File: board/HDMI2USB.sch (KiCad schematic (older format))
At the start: 0 parts

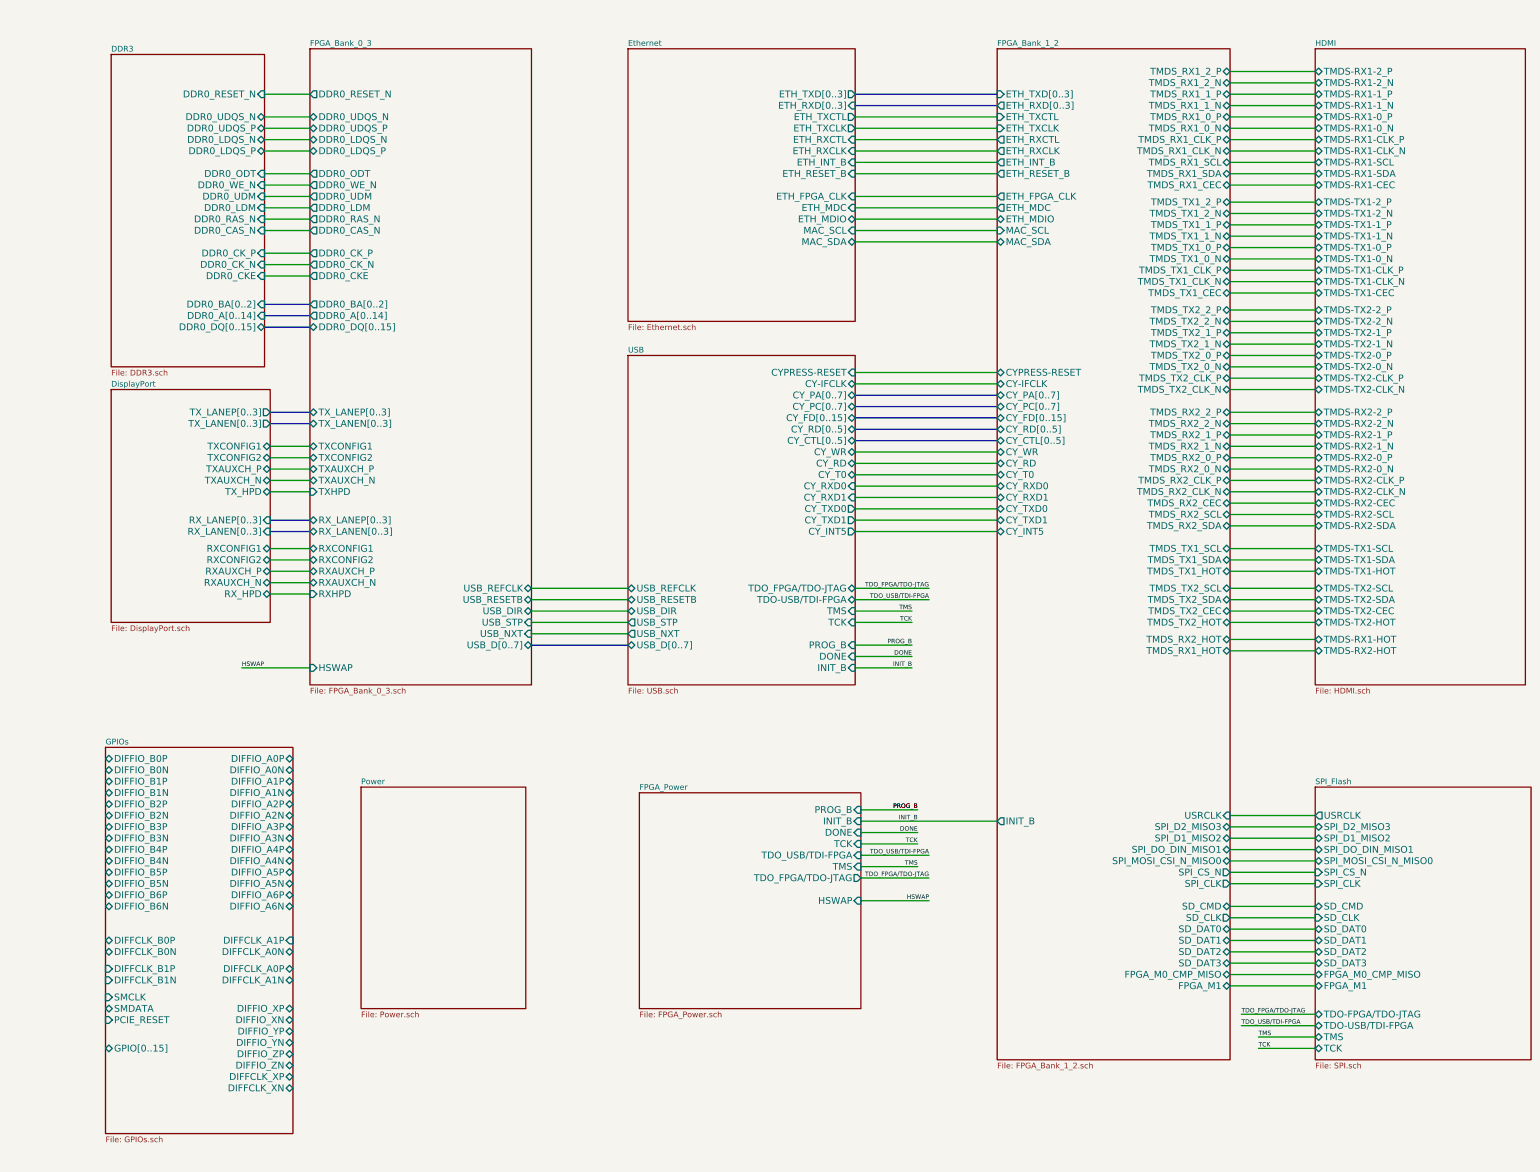
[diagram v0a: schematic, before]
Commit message: Issue #1680 - Bank 0 Ios
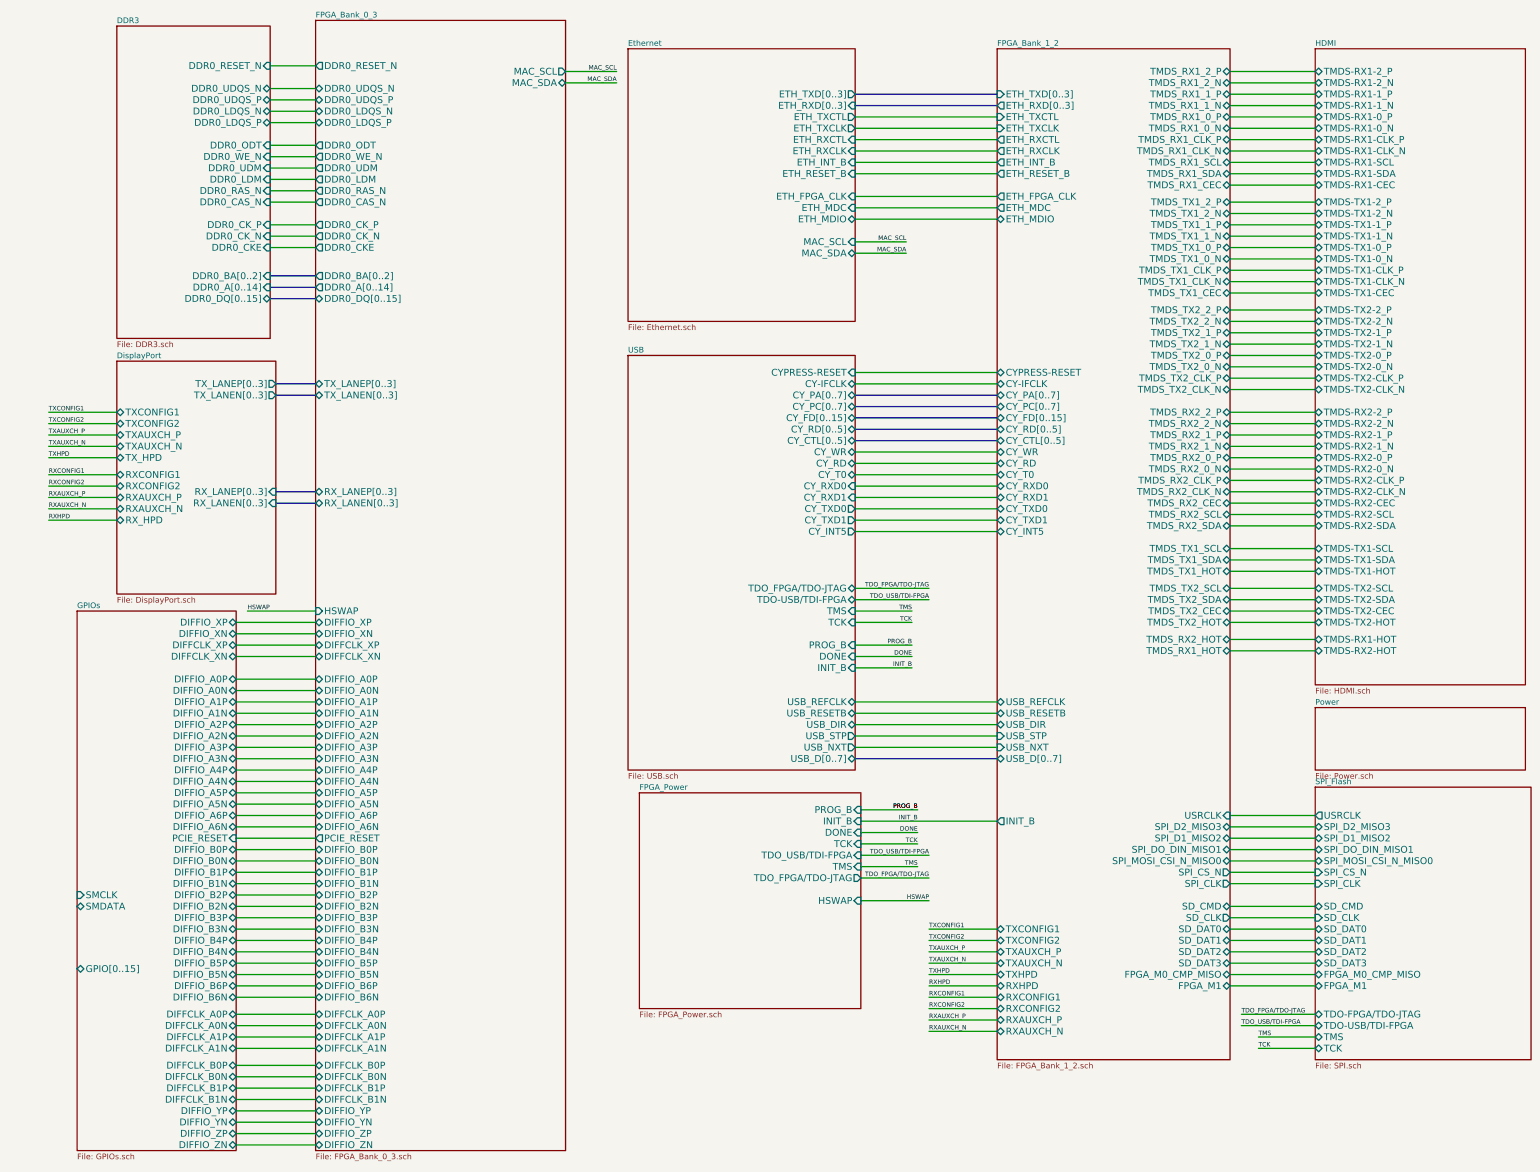
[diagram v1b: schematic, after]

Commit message: Issue #1683
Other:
- note added: "BANK0"
- note added: "BANK1"
- note added: "BANK2"
- note added: "BANK3"
- note added: "CYPRESS/OTG"
- note added: "CYPRESS\nHDMI RX 1\nHDMI RX 2"
- note added: "DDR3"
- note added: "DISPLAY PORT"
- note added: "ETHERNET"
- note added: "FPGA VCC/CONFIG"
- note added: "GTP"
- note added: "HDMI"
- note added: "HDMI TX 1\nHDMI TX 2\nETHERNET\nUTMI\nSPI\nSD\n\n"
- note added: "PCIe GPIOs"
- note added: "PCIe \nGPIOs"
- note added: "POWER SUPPLY"
- note added: "SPI/SD/\nJTAG/\nCRYSTAL"
- note added: "VCCAUX- 3V3\nVCCO_0- 3V3\nVCCO_1- 3V3\nVCCO_2- 3V3\nVCCO_3- 1V5"

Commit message: Issue #1670
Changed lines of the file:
@@
 Sheet 1 12
 Title "HDMI2USB"
-Date "25 mar 2015"
+Date "30 mar 2015"
 Rev "Rev2"
 Comp ""
@@
 F10 "DPTX_HPD" B L 1700 4700 60
 F11 "DPRX_HPD" B L 1700 5250 60
-F12 "RX_LANEP[0..3]" I R 3250 5000 60
-F13 "RX_LANEN[0..3]" I R 3250 5100 60
-F14 "TX_LANEP[0..3]" O R 3250 4050 60
-F15 "TX_LANEN[0..3]" O R 3250 4150 60
+F12 "DPRX_LANEP[0..3]" B R 3250 5250 60
+F13 "DPRX_LANEN[0..3]" B R 3250 5350 60
+F14 "DPTX_LANEP[0..3]" B R 3250 4050 60
+F15 "DPTX_LANEN[0..3]" B R 3250 4150 60
 $EndSheet
 $Sheet
@@
 Wire Bus Line
 	3250 4150 3800 4150
-Wire Bus Line
-	3250 5100 3800 5100
-Wire Bus Line
-	3450 5000 3800 5000
 Wire Wire Line
 	8550 5150 9800 5150
@@
 Text Label 1100 5250 0    39   ~ 0
 DPRXHPD
-Wire Bus Line
-	3250 5000 3500 5000
 $Sheet
 S 3800 850  2200 9950
@@
 F18 "DDR0_CKE" O L 3800 2850 60
 F19 "HSWAP" I L 3800 6050 60
-F20 "RX_LANEN[0..3]" B L 3800 5100 60
-F21 "RX_LANEP[0..3]" B L 3800 5000 60
-F22 "TX_LANEN[0..3]" B L 3800 4150 60
-F23 "TX_LANEP[0..3]" B L 3800 4050 60
-F24 "DIFFIO_B0P" B L 3800 8150 60
-F25 "DIFFIO_B1P" B L 3800 8350 60
-F26 "DIFFIO_B2P" B L 3800 8550 60
-F27 "DIFFIO_B3P" B L 3800 8750 60
-F28 "DIFFIO_B4P" B L 3800 8950 60
-F29 "DIFFIO_B5P" B L 3800 9150 60
-F30 "DIFFIO_B6P" B L 3800 9350 60
-F31 "DIFFIO_B0N" B L 3800 8250 60
-F32 "DIFFIO_B1N" B L 3800 8450 60
-F33 "DIFFIO_B2N" B L 3800 8650 60
-F34 "DIFFIO_B3N" B L 3800 8850 60
-F35 "DIFFIO_B4N" B L 3800 9050 60
-F36 "DIFFIO_B5N" B L 3800 9250 60
-F37 "DIFFIO_B6N" B L 3800 9450 60
-F38 "DIFFIO_A0N" B L 3800 6750 60
-F39 "DIFFIO_A1N" B L 3800 6950 60
-F40 "DIFFIO_A2N" B L 3800 7150 60
-F41 "DIFFIO_A3N" B L 3800 7350 60
-F42 "DIFFIO_A4N" B L 3800 7550 60
-F43 "DIFFIO_A5N" B L 3800 7750 60
-F44 "DIFFIO_A6N" B L 3800 7950 60
-F45 "DIFFIO_A0P" B L 3800 6650 60
-F46 "DIFFIO_A1P" B L 3800 6850 60
-F47 "DIFFIO_A2P" B L 3800 7050 60
-F48 "DIFFIO_A3P" B L 3800 7250 60
-F49 "DIFFIO_A4P" B L 3800 7450 60
-F50 "DIFFIO_A5P" B L 3800 7650 60
-F51 "DIFFIO_A6P" B L 3800 7850 60
-F52 "DIFFCLK_B0P" B L 3800 10050 60
-F53 "DIFFCLK_B1P" B L 3800 10250 60
-F54 "DIFFCLK_B0N" B L 3800 10150 60
-F55 "DIFFCLK_B1N" B L 3800 10350 60
-F56 "DIFFCLK_A0N" B L 3800 9700 60
-F57 "DIFFCLK_A1N" B L 3800 9900 60
-F58 "DIFFCLK_A0P" B L 3800 9600 60
-F59 "DIFFCLK_A1P" B L 3800 9800 60
-F60 "DIFFIO_ZN" B L 3800 10750 60
-F61 "DIFFIO_ZP" B L 3800 10650 60
-F62 "DIFFIO_XN" B L 3800 6250 60
-F63 "DIFFIO_XP" B L 3800 6150 60
-F64 "DIFFIO_YN" B L 3800 10550 60
-F65 "DIFFIO_YP" B L 3800 10450 60
-F66 "PCIE_RESET" O L 3800 8050 60
-F67 "DIFFCLK_XP" B L 3800 6350 60
-F68 "DIFFCLK_XN" B L 3800 6450 60
-F69 "MAC_SCL" O R 6000 3500 60
-F70 "MAC_SDA" B R 6000 3600 60
+F20 "DPRX_LANEN[0..3]" B L 3800 5350 60
+F21 "DPTX_LANEN[0..3]" B L 3800 4150 60
+F22 "DPTX_LANEP[0..3]" B L 3800 4050 60
+F23 "DIFFIO_B0P" B L 3800 8150 60
+F24 "DIFFIO_B1P" B L 3800 8350 60
+F25 "DIFFIO_B2P" B L 3800 8550 60
+F26 "DIFFIO_B3P" B L 3800 8750 60
+F27 "DIFFIO_B4P" B L 3800 8950 60
+F28 "DIFFIO_B5P" B L 3800 9150 60
+F29 "DIFFIO_B6P" B L 3800 9350 60
+F30 "DIFFIO_B0N" B L 3800 8250 60
+F31 "DIFFIO_B1N" B L 3800 8450 60
+F32 "DIFFIO_B2N" B L 3800 8650 60
+F33 "DIFFIO_B3N" B L 3800 8850 60
+F34 "DIFFIO_B4N" B L 3800 9050 60
+F35 "DIFFIO_B5N" B L 3800 9250 60
+F36 "DIFFIO_B6N" B L 3800 9450 60
+F37 "DIFFIO_A0N" B L 3800 6750 60
+F38 "DIFFIO_A1N" B L 3800 6950 60
+F39 "DIFFIO_A2N" B L 3800 7150 60
+F40 "DIFFIO_A3N" B L 3800 7350 60
+F41 "DIFFIO_A4N" B L 3800 7550 60
+F42 "DIFFIO_A5N" B L 3800 7750 60
+F43 "DIFFIO_A6N" B L 3800 7950 60
+F44 "DIFFIO_A0P" B L 3800 6650 60
+F45 "DIFFIO_A1P" B L 3800 6850 60
+F46 "DIFFIO_A2P" B L 3800 7050 60
+F47 "DIFFIO_A3P" B L 3800 7250 60
+F48 "DIFFIO_A4P" B L 3800 7450 60
+F49 "DIFFIO_A5P" B L 3800 7650 60
+F50 "DIFFIO_A6P" B L 3800 7850 60
+F51 "DIFFCLK_B0P" B L 3800 10050 60
+F52 "DIFFCLK_B1P" B L 3800 10250 60
+F53 "DIFFCLK_B0N" B L 3800 10150 60
+F54 "DIFFCLK_B1N" B L 3800 10350 60
+F55 "DIFFCLK_A0N" B L 3800 9700 60
+F56 "DIFFCLK_A1N" B L 3800 9900 60
+F57 "DIFFCLK_A0P" B L 3800 9600 60
+F58 "DIFFCLK_A1P" B L 3800 9800 60
+F59 "DIFFIO_ZN" B L 3800 10750 60
+F60 "DIFFIO_ZP" B L 3800 10650 60
+F61 "DIFFIO_XN" B L 3800 6250 60
+F62 "DIFFIO_XP" B L 3800 6150 60
+F63 "DIFFIO_YN" B L 3800 10550 60
+F64 "DIFFIO_YP" B L 3800 10450 60
+F65 "PCIE_RESET" O L 3800 8050 60
+F66 "DIFFCLK_XP" B L 3800 6350 60
+F67 "DIFFCLK_XN" B L 3800 6450 60
+F68 "MAC_SCL" O R 6000 3500 60
+F69 "MAC_SDA" B R 6000 3600 60
+F70 "DPRX_LANEP[0..3]" B L 3800 5250 60
 $EndSheet
 Wire Wire Line
@@
 	6000 3600 6450 3600
 Connection ~ 6450 3600
+Wire Bus Line
+	3250 5250 3800 5250
+Wire Bus Line
+	3250 5350 3800 5350
 $EndSCHEMATC

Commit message: Issue #1647 - Final changes
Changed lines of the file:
@@
 LIBS:contrib
 LIBS:valves
+LIBS:hdmi2usb
+LIBS:timvideos-pcie-8x
 LIBS:HDMI2USB-cache
 EELAYER 27 0
@@
 Sheet 1 12
 Title "HDMI2USB"
-Date "1 apr 2015"
+Date "2 apr 2015"
 Rev "Rev2"
 Comp ""
@@
 F24 "PCIO2" B L 12600 10250 60
 F25 "PCIO3" B L 12600 10350 60
+F26 "CYPRESS_RESET" O L 12600 9500 60
 $EndSheet
 $Sheet
@@
 Text Label 1100 8650 0    39   ~ 0
 SMDATA
+Text Label 9550 3950 2    39   ~ 0
+CYPRESS-RESET
+Text Label 11950 9500 0    39   ~ 0
+CYPRESS-RESET
+Wire Wire Line
+	11950 9500 12600 9500
 $EndSCHEMATC

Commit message: Issue #1713
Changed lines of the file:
@@
 Sheet 1 12
 Title "HDMI2USB"
-Date "2 apr 2015"
+Date "7 apr 2015"
 Rev "Rev2"
 Comp ""
@@
 F46 "TMDS-TX2-SDA" B L 12600 5950 60
 F47 "TMDS-TX2-HOT" B L 12600 6150 60
-F48 "TMDS-RX1-HOT" B L 12600 6300 60
-F49 "TMDS-RX2-HOT" B L 12600 6400 60
+F48 "TMDS-RX1-HOT" B L 12600 6400 60
+F49 "TMDS-RX2-HOT" B L 12600 6300 60
 $EndSheet
 Wire Wire Line

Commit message: Issue #1546
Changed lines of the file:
@@
 Sheet 1 12
 Title "HDMI2USB"
-Date "8 apr 2015"
+Date "10 apr 2015"
 Rev "Rev2"
 Comp ""
@@
 F24 "PCIO2" B L 12600 10250 60
 F25 "PCIO3" B L 12600 10350 60
-F26 "CYPRESS_RESET" O L 12600 9500 60
+F26 "RST" O L 12600 9500 60
 $EndSheet
 $Sheet
@@
 F30 "MAC_SDA" B L 6550 4000 60
 F31 "MAC_SCL" I L 6550 4100 60
+F32 "RST" I R 8550 6650 60
 $EndSheet
 Wire Wire Line
@@
 Text Label 9550 3950 2    39   ~ 0
 CYPRESS-RESET
-Text Label 11950 9500 0    39   ~ 0
-CYPRESS-RESET
-Wire Wire Line
-	11950 9500 12600 9500
+Text Label 12100 9500 0    39   ~ 0
+RST
+Text Label 9050 6650 2    39   ~ 0
+RST
+Wire Wire Line
+	9050 6650 8550 6650
+Wire Wire Line
+	12100 9500 12600 9500
 $EndSCHEMATC
